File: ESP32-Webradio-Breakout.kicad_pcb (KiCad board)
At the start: 2 copper layers, 80 x 60 mm, 35 parts, among them J1 AudioJack, J2 Conn_01x02, Q1 BC547, SW1 RotaryEncoder_Switch, U1 ESP32NodeMCU, U2 PCF8574, U3 DS18B20

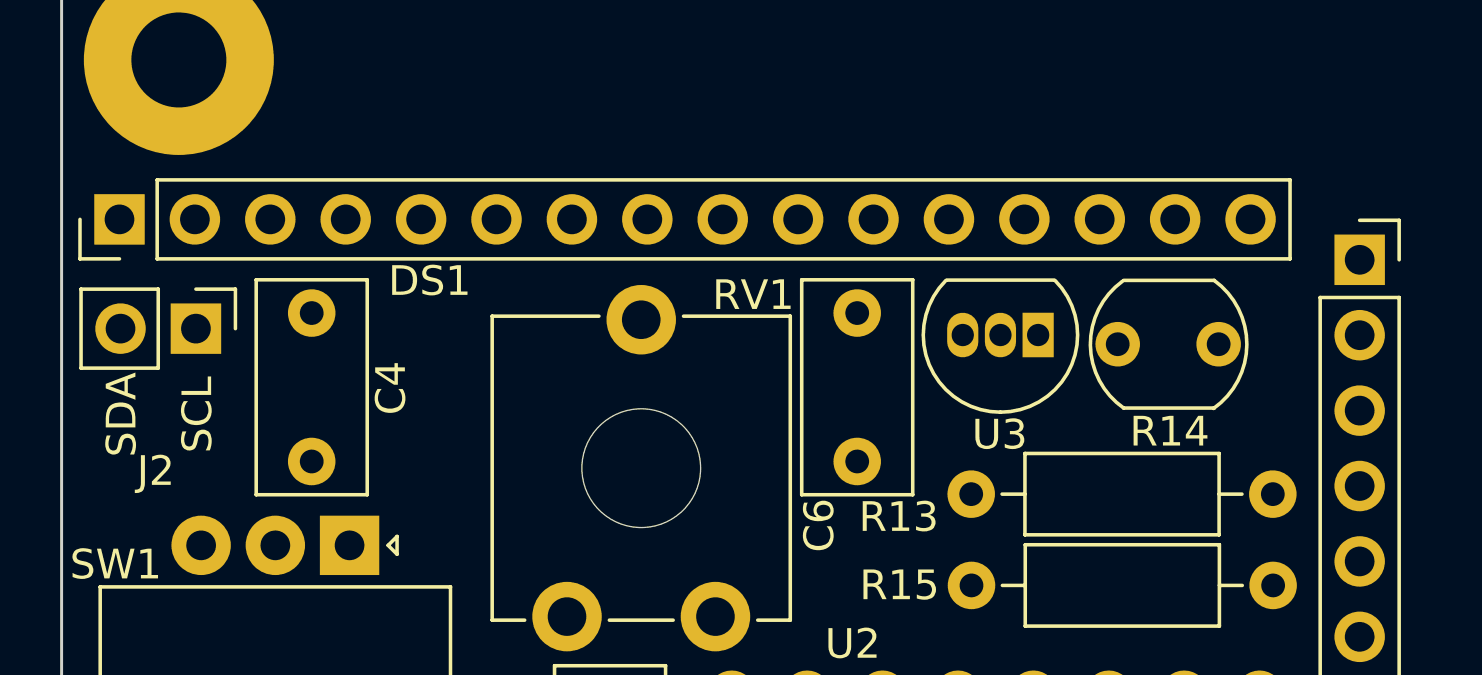
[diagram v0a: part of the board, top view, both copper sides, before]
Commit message: Rotated display connector 180 degrees
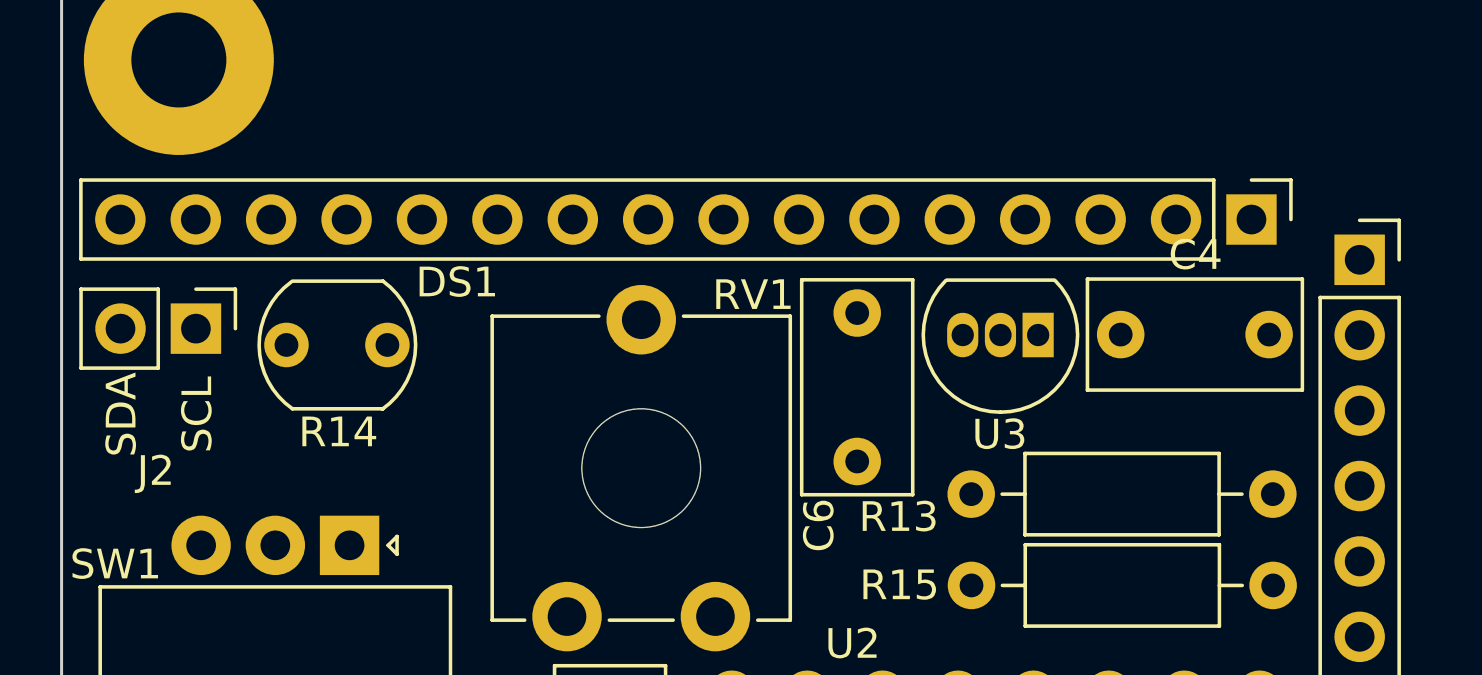
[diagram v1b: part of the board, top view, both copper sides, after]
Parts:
- moved DS1 38.1 mm to (135.9, 46.2), turned to -90 degrees
- moved R14 28.0 mm to (106.8, 50.5)
- moved C4 27.3 mm to (131.5, 50.1), turned to 0 degrees
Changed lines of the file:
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@@
   )
   (footprint "Capacitor_THT:C_Rect_L7.0mm_W3.5mm_P5.00mm" (layer "F.Cu")
-    (at 104.225 49.375 -90)
+    (at 131.475 50.1)
     (descr "C, Rect series, Radial, pin pitch=5.00mm, , length*width=7*3.5mm^2, Capacitor")
     (tags "C Rect series Radial pin pitch 5.00mm  length 7mm width 3.5mm Capacitor")
@@
     (property "Sheetname" "")
     (attr through_hole)
-    (fp_text reference "C4" (at 2.525 -2.675 90) (layer "F.SilkS")
-      (effects (font (size 1 1) (thickness 0.15)))
-    )
-    (fp_text value "100n" (at 2.5 3 90) (layer "F.Fab")
-      (effects (font (size 1 1) (thickness 0.15)))
-    )
-    (fp_text user "${REFERENCE}" (at 2.5 0 90) (layer "F.Fab")
+    (fp_text reference "C4" (at 2.525 -2.675) (layer "F.SilkS")
+      (effects (font (size 1 1) (thickness 0.15)))
+    )
+    (fp_text value "100n" (at 2.5 3) (layer "F.Fab")
+      (effects (font (size 1 1) (thickness 0.15)))
+    )
+    (fp_text user "${REFERENCE}" (at 2.5 0) (layer "F.Fab")
       (effects (font (size 1 1) (thickness 0.15)))
     )
@@
     (fp_line (start -1 1.75) (end 6 1.75) (layer "F.Fab") (width 0.1))
     (fp_line (start -1 -1.75) (end -1 1.75) (layer "F.Fab") (width 0.1))
-    (pad "1" thru_hole circle (at 0 0 270) (size 1.6 1.6) (drill 0.8) (layers *.Cu *.Mask)
+    (pad "1" thru_hole circle (at 0 0) (size 1.6 1.6) (drill 0.8) (layers *.Cu *.Mask)
       (net 10 "+5V") (pintype "passive"))
-    (pad "2" thru_hole circle (at 5 0 270) (size 1.6 1.6) (drill 0.8) (layers *.Cu *.Mask)
+    (pad "2" thru_hole circle (at 5 0) (size 1.6 1.6) (drill 0.8) (layers *.Cu *.Mask)
       (net 9 "GND") (pintype "passive"))
     (model "${KICAD6_3DMODEL_DIR}/Capacitor_THT.3dshapes/C_Rect_L7.0mm_W3.5mm_P5.00mm.wrl"
@@
   )
   (footprint "OptoDevice:R_LDR_5.1x4.3mm_P3.4mm_Vertical" (layer "F.Cu")
-    (at 134.775 50.425 180)
+    (at 106.775 50.45 180)
     (descr "Resistor, LDR 5.1x3.4mm, see http://yourduino.com/docs/Photoresistor-5516-datasheet.pdf")
     (tags "Resistor LDR5.1x3.4mm")
@@
   )
   (footprint "Connector_PinHeader_2.54mm:PinHeader_1x16_P2.54mm_Vertical" (layer "F.Cu")
-    (at 97.75 46.22 90)
+    (at 135.88 46.225 -90)
     (descr "Through hole straight pin header, 1x16, 2.54mm pitch, single row")
     (tags "Through hole pin header THT 1x16 2.54mm single row")
@@
     (property "Sheetname" "")
     (attr through_hole)
-    (fp_text reference "DS1" (at -2.08 10.45) (layer "F.SilkS")
+    (fp_text reference "DS1" (at 2.125 26.755) (layer "F.SilkS")
       (effects (font (size 1 1) (thickness 0.15)))
     )
@@
     (fp_line (start 1.27 39.37) (end -1.27 39.37) (layer "F.Fab") (width 0.1))
     (fp_line (start -0.635 -1.27) (end 1.27 -1.27) (layer "F.Fab") (width 0.1))
-    (pad "1" thru_hole rect (at 0 0 90) (size 1.7 1.7) (drill 1) (layers *.Cu *.Mask)
+    (pad "1" thru_hole rect (at 0 0 270) (size 1.7 1.7) (drill 1) (layers *.Cu *.Mask)
       (net 9 "GND") (pinfunction "VSS") (pintype "power_in"))
-    (pad "2" thru_hole oval (at 0 2.54 90) (size 1.7 1.7) (drill 1) (layers *.Cu *.Mask)
+    (pad "2" thru_hole oval (at 0 2.54 270) (size 1.7 1.7) (drill 1) (layers *.Cu *.Mask)
       (net 10 "+5V") (pinfunction "VDD") (pintype "power_in"))
-    (pad "3" thru_hole oval (at 0 5.08 90) (size 1.7 1.7) (drill 1) (layers *.Cu *.Mask)
+    (pad "3" thru_hole oval (at 0 5.08 270) (size 1.7 1.7) (drill 1) (layers *.Cu *.Mask)
       (net 13 "Net-(DS1-Pad3)") (pinfunction "VO") (pintype "input"))
-    (pad "4" thru_hole oval (at 0 7.62 90) (size 1.7 1.7) (drill 1) (layers *.Cu *.Mask)
+    (pad "4" thru_hole oval (at 0 7.62 270) (size 1.7 1.7) (drill 1) (layers *.Cu *.Mask)
       (net 42 "/P0") (pinfunction "RS") (pintype "input"))
-    (pad "5" thru_hole oval (at 0 10.16 90) (size 1.7 1.7) (drill 1) (layers *.Cu *.Mask)
+    (pad "5" thru_hole oval (at 0 10.16 270) (size 1.7 1.7) (drill 1) (layers *.Cu *.Mask)
       (net 14 "Net-(DS1-Pad5)") (pinfunction "R/W") (pintype "input"))
-    (pad "6" thru_hole oval (at 0 12.7 90) (size 1.7 1.7) (drill 1) (layers *.Cu *.Mask)
+    (pad "6" thru_hole oval (at 0 12.7 270) (size 1.7 1.7) (drill 1) (layers *.Cu *.Mask)
       (net 43 "/P2") (pinfunction "E") (pintype "input"))
-    (pad "7" thru_hole oval (at 0 15.24 90) (size 1.7 1.7) (drill 1) (layers *.Cu *.Mask)
+    (pad "7" thru_hole oval (at 0 15.24 270) (size 1.7 1.7) (drill 1) (layers *.Cu *.Mask)
       (net 44 "unconnected-(DS1-Pad7)") (pinfunction "D0") (pintype "input+no_connect"))
-    (pad "8" thru_hole oval (at 0 17.78 90) (size 1.7 1.7) (drill 1) (layers *.Cu *.Mask)
+    (pad "8" thru_hole oval (at 0 17.78 270) (size 1.7 1.7) (drill 1) (layers *.Cu *.Mask)
       (net 45 "unconnected-(DS1-Pad8)") (pinfunction "D1") (pintype "input+no_connect"))
-    (pad "9" thru_hole oval (at 0 20.32 90) (size 1.7 1.7) (drill 1) (layers *.Cu *.Mask)
+    (pad "9" thru_hole oval (at 0 20.32 270) (size 1.7 1.7) (drill 1) (layers *.Cu *.Mask)
       (net 46 "unconnected-(DS1-Pad9)") (pinfunction "D2") (pintype "input+no_connect"))
-    (pad "10" thru_hole oval (at 0 22.86 90) (size 1.7 1.7) (drill 1) (layers *.Cu *.Mask)
+    (pad "10" thru_hole oval (at 0 22.86 270) (size 1.7 1.7) (drill 1) (layers *.Cu *.Mask)
       (net 47 "unconnected-(DS1-Pad10)") (pinfunction "D3") (pintype "input+no_connect"))
-    (pad "11" thru_hole oval (at 0 25.4 90) (size 1.7 1.7) (drill 1) (layers *.Cu *.Mask)
+    (pad "11" thru_hole oval (at 0 25.4 270) (size 1.7 1.7) (drill 1) (layers *.Cu *.Mask)
       (net 15 "Net-(DS1-Pad11)") (pinfunction "D4") (pintype "input"))
-    (pad "12" thru_hole oval (at 0 27.94 90) (size 1.7 1.7) (drill 1) (layers *.Cu *.Mask)
+    (pad "12" thru_hole oval (at 0 27.94 270) (size 1.7 1.7) (drill 1) (layers *.Cu *.Mask)
       (net 19 "Net-(DS1-Pad12)") (pinfunction "D5") (pintype "input"))
-    (pad "13" thru_hole oval (at 0 30.48 90) (size 1.7 1.7) (drill 1) (layers *.Cu *.Mask)
+    (pad "13" thru_hole oval (at 0 30.48 270) (size 1.7 1.7) (drill 1) (layers *.Cu *.Mask)
       (net 21 "Net-(DS1-Pad13)") (pinfunction "D6") (pintype "input"))
-    (pad "14" thru_hole oval (at 0 33.02 90) (size 1.7 1.7) (drill 1) (layers *.Cu *.Mask)
+    (pad "14" thru_hole oval (at 0 33.02 270) (size 1.7 1.7) (drill 1) (layers *.Cu *.Mask)
       (net 22 "Net-(DS1-Pad14)") (pinfunction "D7") (pintype "input"))
-    (pad "15" thru_hole oval (at 0 35.56 90) (size 1.7 1.7) (drill 1) (layers *.Cu *.Mask)
+    (pad "15" thru_hole oval (at 0 35.56 270) (size 1.7 1.7) (drill 1) (layers *.Cu *.Mask)
       (net 10 "+5V") (pinfunction "LED(+)") (pintype "power_in"))
-    (pad "16" thru_hole oval (at 0 38.1 90) (size 1.7 1.7) (drill 1) (layers *.Cu *.Mask)
+    (pad "16" thru_hole oval (at 0 38.1 270) (size 1.7 1.7) (drill 1) (layers *.Cu *.Mask)
       (net 23 "Net-(DS1-Pad16)") (pinfunction "LED(-)") (pintype "power_in"))
     (model "${KICAD6_3DMODEL_DIR}/Connector_PinHeader_2.54mm.3dshapes/PinHeader_1x16_P2.54mm_Vertical.wrl"

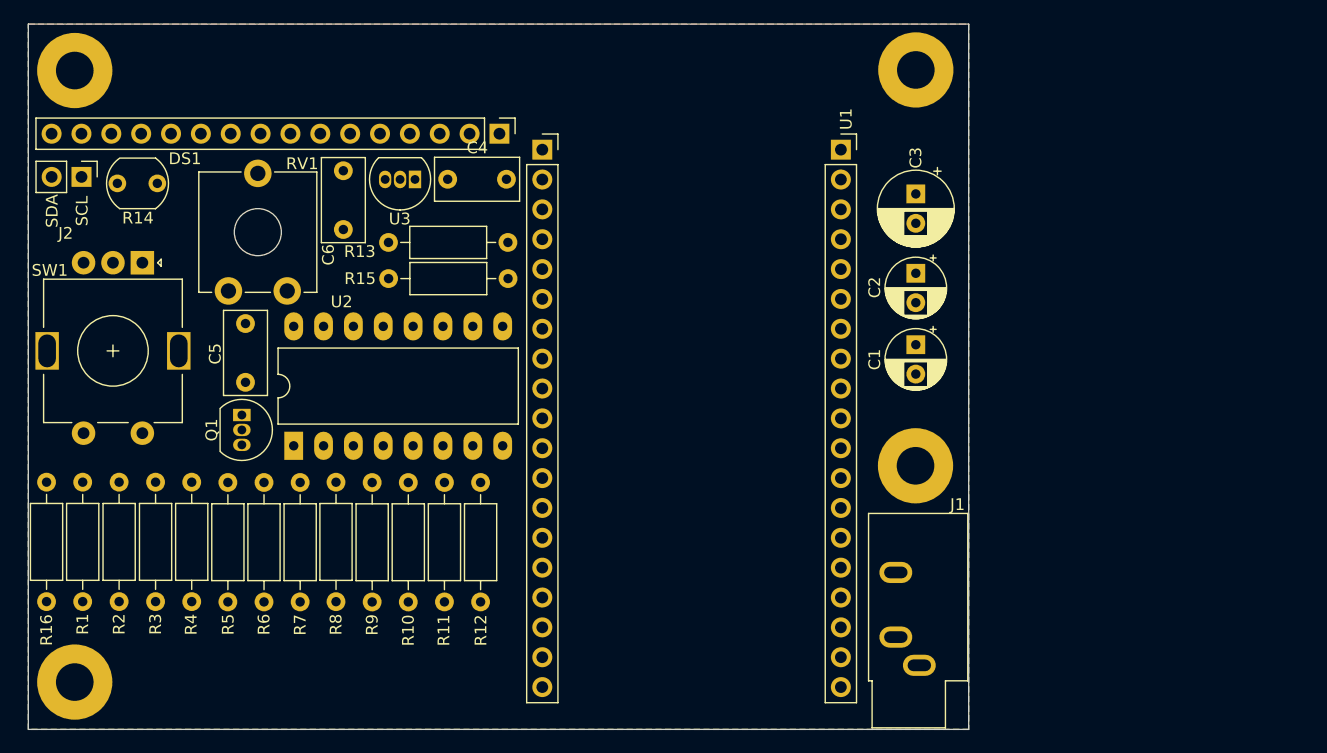
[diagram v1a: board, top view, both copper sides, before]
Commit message: Flipped left and right for a better display connection
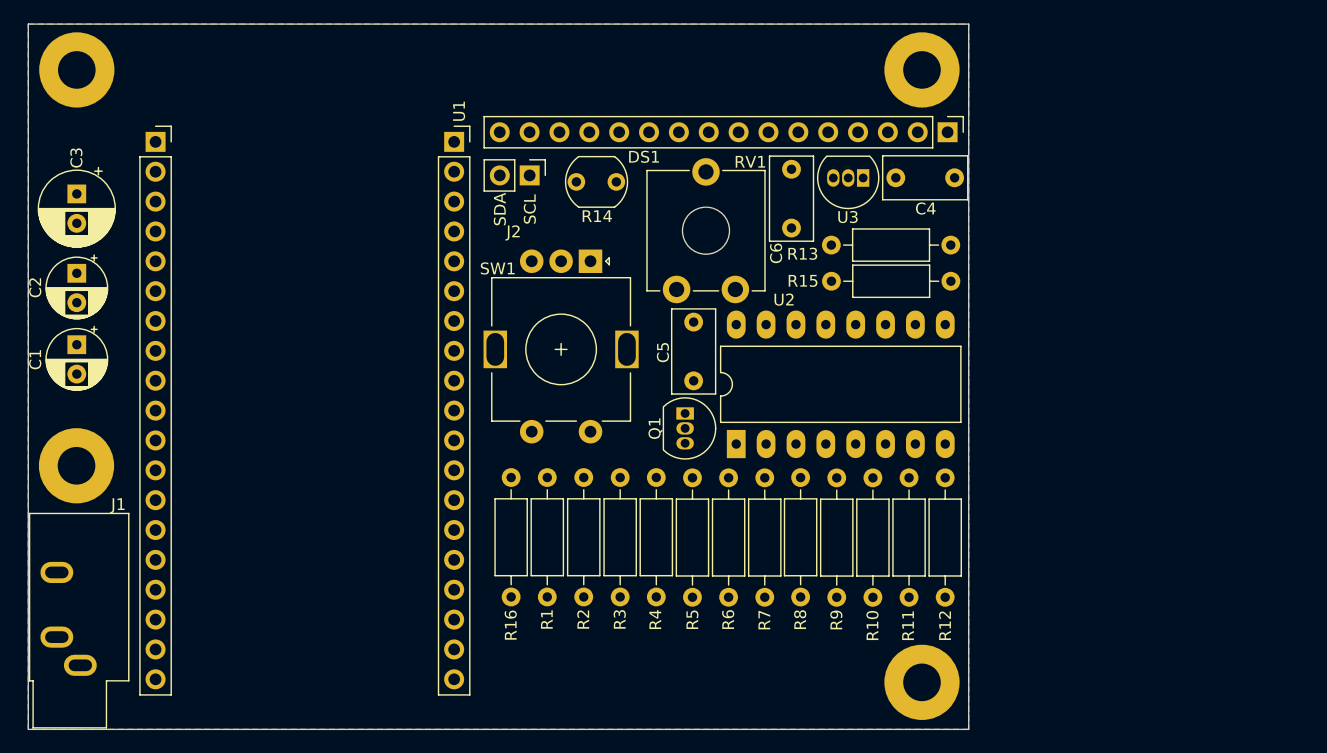
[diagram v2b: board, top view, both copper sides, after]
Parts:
- moved REF** 72.1 mm to (171.8, 40.8)
- moved REF** 72.1 mm to (171.8, 92.9)
- moved C1 71.4 mm to (99.9, 64.2)
- moved C2 71.4 mm to (99.9, 58.1)
- moved C3 71.4 mm to (99.9, 51.3)
- moved REF** 71.4 mm to (99.9, 40.8)
- moved J1 71.4 mm to (100.2, 91.5)
- moved REF** 71.4 mm to (99.9, 74.5)
- moved R10 39.5 mm to (167.7, 85.7)
- moved R11 39.5 mm to (170.7, 85.7)
- moved R12 39.5 mm to (173.8, 85.7)
- moved R16 39.5 mm to (136.9, 75.5)
- moved R2 39.5 mm to (143.1, 85.6)
- moved R3 39.5 mm to (146.2, 85.6)
- moved R5 39.5 mm to (152.3, 75.5)
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
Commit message: Added pin for touch sensor Some regrouping
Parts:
- added J2: Conn_01x01, Connector_PinHeader_2.54mm:PinHeader_1x01_P2.54mm_Vertical, F.Cu at (137.2, 91.5)
- renumbered J2 to J3
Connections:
- R1 pad 1: +3V3 -> Net-(R1-Pad1)
- R3 pad 1: +3V3 -> Net-(R1-Pad1)
- U1 pad 26: unconnected-(U1-Pad26) -> /Touch_Sens
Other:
- board text added: "TOUCH"
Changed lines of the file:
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@@
   (net 36 "/SCL")
   (net 37 "unconnected-(U1-Pad25)")
-  (net 38 "unconnected-(U1-Pad26)")
+  (net 38 "/Touch_Sens")
   (net 39 "/SDA")
   (net 40 "unconnected-(U1-Pad27)")
@@
   (net 58 "unconnected-(U1-Pad37)")
   (net 59 "unconnected-(U2-Pad7)")
+  (net 60 "Net-(R1-Pad1)")
   (footprint "Resistor_THT:R_Axial_DIN0207_L6.3mm_D2.5mm_P10.16mm_Horizontal" (layer "F.Cu")
     (at 158.45 85.66 90)
@@
     (fp_line (start 0 0) (end 1.93 0) (layer "F.Fab") (width 0.1))
     (pad "1" thru_hole circle (at 0 0 90) (size 1.6 1.6) (drill 0.8) (layers *.Cu *.Mask)
-      (net 1 "+3V3") (pintype "passive"))
+      (net 60 "Net-(R1-Pad1)") (pintype "passive"))
     (pad "2" thru_hole oval (at 10.16 0 90) (size 1.6 1.6) (drill 0.8) (layers *.Cu *.Mask)
       (net 7 "/Enc_B") (pintype "passive"))
@@
     (descr "Mounting Hole 3.2mm, M3")
     (tags "mounting hole 3.2mm m3")
-    (attr board_only exclude_from_pos_files exclude_from_bom)
+    (attr board_only exclude_from_bom)
     (fp_text reference "REF**" (at 0 -4.2 90) (layer "F.SilkS") hide
       (effects (font (size 1 1) (thickness 0.15)))
@@
     (descr "Mounting Hole 3.2mm, M3")
     (tags "mounting hole 3.2mm m3")
-    (attr board_only exclude_from_pos_files exclude_from_bom)
+    (attr board_only exclude_from_bom)
     (fp_text reference "REF**" (at 0 -4.2 90) (layer "F.SilkS") hide
       (effects (font (size 1 1) (thickness 0.15)))
@@
     )
   )
+  (footprint "Connector_PinHeader_2.54mm:PinHeader_1x01_P2.54mm_Vertical" (layer "F.Cu")
+    (at 137.15 91.5)
+    (descr "Through hole straight pin header, 1x01, 2.54mm pitch, single row")
+    (tags "Through hole pin header THT 1x01 2.54mm single row")
+    (property "Sheetfile" "ESP32-Webradio-Breakout.kicad_sch")
+    (property "Sheetname" "")
+    (attr through_hole)
+    (fp_text reference "J2" (at 2.3 0.15) (layer "F.SilkS")
+      (effects (font (size 1 1) (thickness 0.15)))
+    )
+    (fp_text value "Conn_01x01" (at 0 2.33) (layer "F.Fab")
+      (effects (font (size 1 1) (thickness 0.15)))
+    )
+    (fp_text user "${REFERENCE}" (at 0 0 90) (layer "F.Fab")
+      (effects (font (size 1 1) (thickness 0.15)))
+    )
+    (fp_line (start -1.33 -1.33) (end 0 -1.33) (layer "F.SilkS") (width 0.12))
+    (fp_line (start -1.33 0) (end -1.33 -1.33) (layer "F.SilkS") (width 0.12))
+    (fp_line (start -1.33 1.27) (end 1.33 1.27) (layer "F.SilkS") (width 0.12))
+    (fp_line (start -1.33 1.27) (end -1.33 1.33) (layer "F.SilkS") (width 0.12))
+    (fp_line (start 1.33 1.27) (end 1.33 1.33) (layer "F.SilkS") (width 0.12))
+    (fp_line (start -1.33 1.33) (end 1.33 1.33) (layer "F.SilkS") (width 0.12))
+    (fp_line (start 1.8 -1.8) (end -1.8 -1.8) (layer "F.CrtYd") (width 0.05))
+    (fp_line (start -1.8 -1.8) (end -1.8 1.8) (layer "F.CrtYd") (width 0.05))
+    (fp_line (start -1.8 1.8) (end 1.8 1.8) (layer "F.CrtYd") (width 0.05))
+    (fp_line (start 1.8 1.8) (end 1.8 -1.8) (layer "F.CrtYd") (width 0.05))
+    (fp_line (start -1.27 -0.635) (end -0.635 -1.27) (layer "F.Fab") (width 0.1))
+    (fp_line (start -0.635 -1.27) (end 1.27 -1.27) (layer "F.Fab") (width 0.1))
+    (fp_line (start -1.27 1.27) (end -1.27 -0.635) (layer "F.Fab") (width 0.1))
+    (fp_line (start 1.27 1.27) (end -1.27 1.27) (layer "F.Fab") (width 0.1))
+    (fp_line (start 1.27 -1.27) (end 1.27 1.27) (layer "F.Fab") (width 0.1))
+    (pad "1" thru_hole rect (at 0 0) (size 1.7 1.7) (drill 1) (layers *.Cu *.Mask)
+      (net 38 "/Touch_Sens") (pinfunction "Pin_1") (pintype "passive"))
+    (model "${KICAD6_3DMODEL_DIR}/Connector_PinHeader_2.54mm.3dshapes/PinHeader_1x01_P2.54mm_Vertical.wrl"
+      (offset (xyz 0 0 0))
+      (scale (xyz 1 1 1))
+      (rotate (xyz 0 0 0))
+    )
+  )
   (footprint "Resistor_THT:R_Axial_DIN0207_L6.3mm_D2.5mm_P10.16mm_Horizontal" (layer "F.Cu")
     (at 161.5 85.64 90)
@@
     (fp_line (start 8.23 1.25) (end 8.23 -1.25) (layer "F.Fab") (width 0.1))
     (pad "1" thru_hole circle (at 0 0 90) (size 1.6 1.6) (drill 0.8) (layers *.Cu *.Mask)
-      (net 1 "+3V3") (pintype "passive"))
+      (net 60 "Net-(R1-Pad1)") (pintype "passive"))
     (pad "2" thru_hole oval (at 10.16 0 90) (size 1.6 1.6) (drill 0.8) (layers *.Cu *.Mask)
       (net 16 "/Enc_SW") (pintype "passive"))
@@
     (descr "Mounting Hole 3.2mm, M3")
     (tags "mounting hole 3.2mm m3")
-    (attr board_only exclude_from_pos_files exclude_from_bom)
+    (attr board_only exclude_from_bom)
     (fp_text reference "REF**" (at 0 -4.2) (layer "F.SilkS") hide
       (effects (font (size 1 1) (thickness 0.15)))
@@
     (descr "Mounting Hole 3.2mm, M3")
     (tags "mounting hole 3.2mm m3")
-    (attr board_only exclude_from_pos_files exclude_from_bom)
+    (attr board_only exclude_from_bom)
     (fp_text reference "REF**" (at 0 -4.2) (layer "F.SilkS") hide
       (effects (font (size 1 1) (thickness 0.15)))
@@
     (property "Sheetname" "")
     (attr through_hole)
-    (fp_text reference "J2" (at 4.8 1.35 180) (layer "F.SilkS")
+    (fp_text reference "J3" (at 4.8 1.35 180) (layer "F.SilkS")
       (effects (font (size 1 1) (thickness 0.15)))
     )
@@
       (net 37 "unconnected-(U1-Pad25)") (pinfunction "G0") (pintype "bidirectional+no_connect"))
     (pad "26" thru_hole oval (at 25.4 30.48) (size 1.7 1.7) (drill 1) (layers *.Cu *.Mask)
-      (net 38 "unconnected-(U1-Pad26)") (pinfunction "G4") (pintype "bidirectional+no_connect"))
+      (net 38 "/Touch_Sens") (pinfunction "G4") (pintype "bidirectional"))
     (pad "27" thru_hole oval (at 25.4 27.94) (size 1.7 1.7) (drill 1) (layers *.Cu *.Mask)
       (net 40 "unconnected-(U1-Pad27)") (pinfunction "G16") (pintype "bidirectional+no_connect"))
@@
     (effects (font (size 1 1) (thickness 0.15)))
   )
+  (gr_text "TOUCH" (at 137.2 93.75) (layer "F.SilkS")
+    (effects (font (size 1 1) (thickness 0.15)))
+  )
   (gr_text "SCL" (at 138.5 52.675 90) (layer "F.SilkS")
     (effects (font (size 1 1) (thickness 0.15)))
@@
     )
   )
-  (group "" (id c186418e-e9a0-4ad6-ad1d-bd1d67771eed)
+  (group "Touch" (id ec65b241-cf38-4062-b96c-730d3a1effb6)
     (members
-      142899fd-2046-494f-9822-dff4e6e2ad84
-      53041123-7c40-4275-8165-2d60f21b4127
-      91572389-4c59-4547-bae4-131f20f44d9d
-      9f3d8d52-a82a-4351-98f9-222d21cb955a
-      a19cad61-fb83-43bf-abfb-d02e4e56a3f9
-      db56e9f0-92dd-4ec7-96b2-2e3fa4e59923
-    )
-  )
+      6f9ab252-823c-4606-b51d-5977c98fe8dd
+      99d6dbd6-e093-4094-a938-136d0b567ae2
+    )
+  )
